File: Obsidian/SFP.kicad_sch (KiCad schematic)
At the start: 82 parts, among them J1 TYCO_1888247-1, J11 TYCO_1888247-1, J12 TYCO_1888247-1, J13 TYCO_1888247-1, J8 2180739-1, J9 2180739-1, U17 TCA9535RTWR, U19 TCA9535RTWR, U26 PCA9546ARGV

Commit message: update with available components on LCSC
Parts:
- C19, C23, C27, C28, C35, C36, C37, C38: LCSC (none) -> C296720
- C20, C21, C22, C220, C221, C222, C24, C25, C26, C29, C30, C31, C32, C33, C34, C39, C40, C41, C42: LCSC (none) -> C110251
- J1, J11, J12, J13: LCSC (none) -> C305914
- J8, J9: LCSC (none) -> C42931391
- L2, L3, L4, L5, L6, L7, L8, L9: LCSC (none) -> C82314
- R122, R21, R22, R23, R24, R25, R26, R27, R28, R29, R30, R31, R32, R33, R34, R35, R36, R37, R38, R39, R40, R41, R42, R43, R44, R45, R46, R47, R48: LCSC (none) -> C25900
- R164, R165, R166, R170, R171, R172, R173, R174, R175: LCSC (none) -> C60491
- U17, U19: FT Rotation Offset (none) -> 0; LCSC (none) -> C140277
- U26: FT Rotation Offset (none) -> 0; LCSC (none) -> C2649403

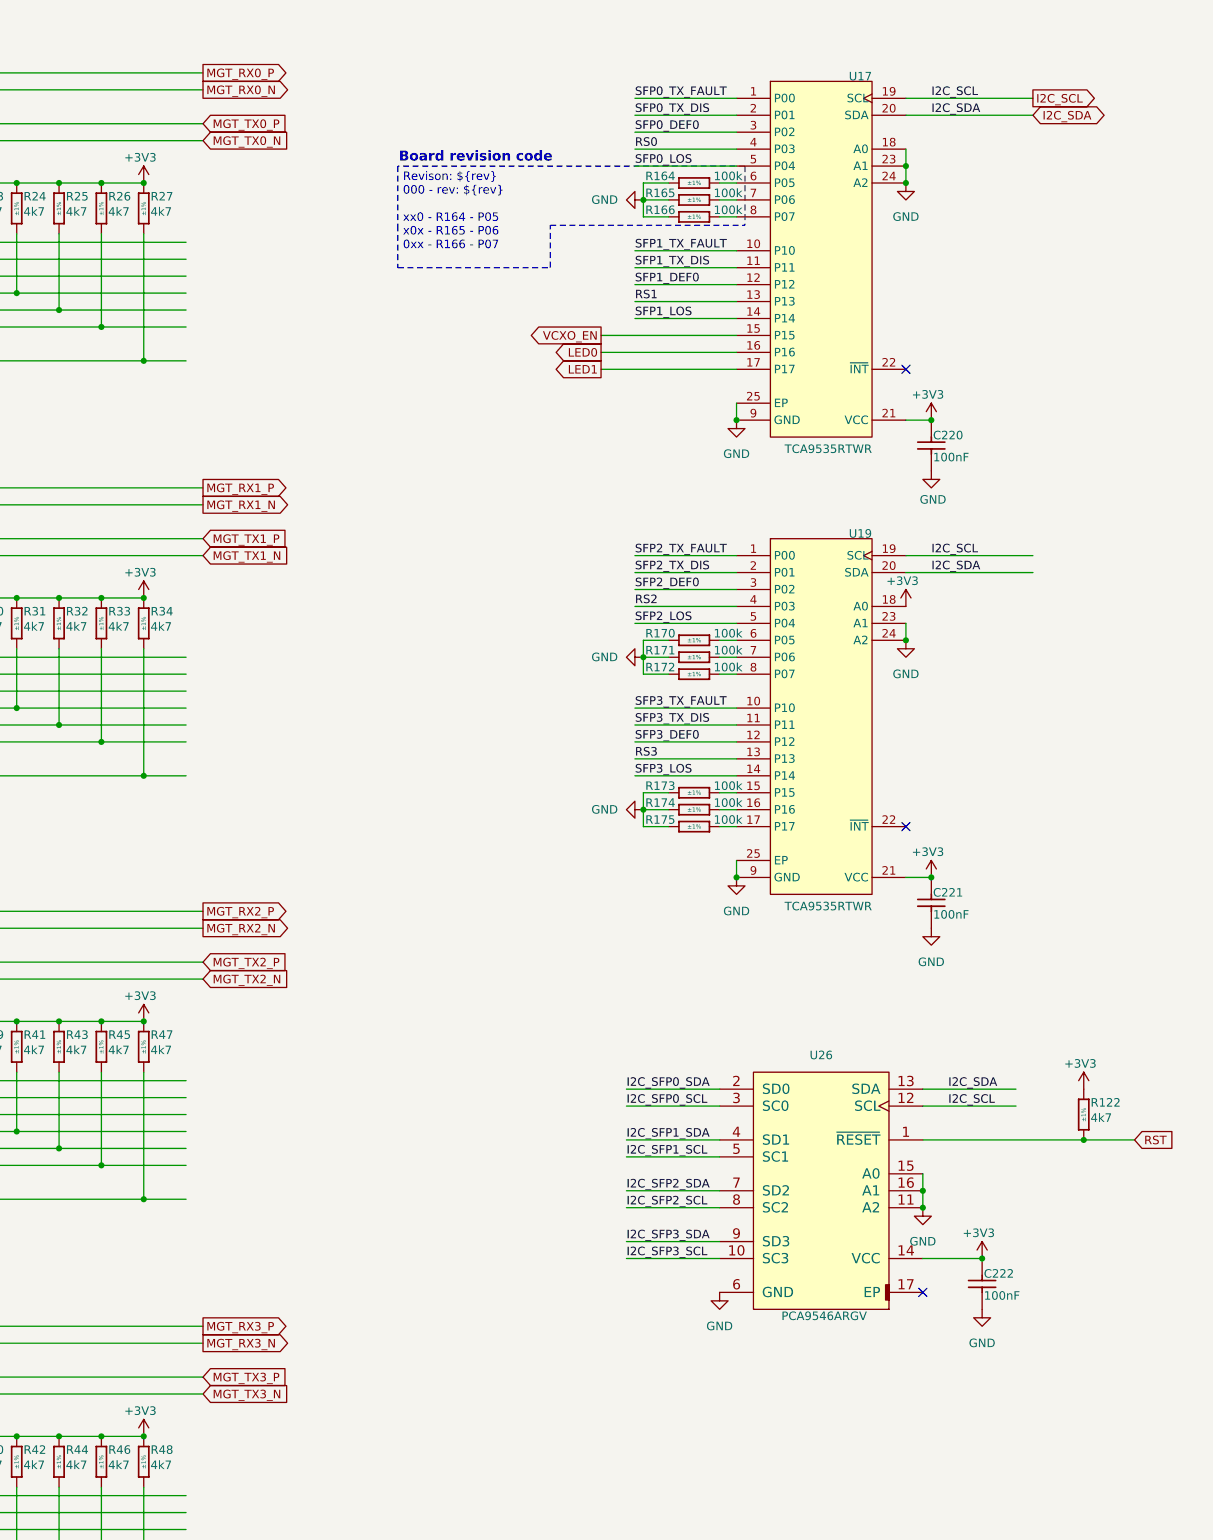
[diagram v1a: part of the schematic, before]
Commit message: replacing global label with hierarchical label
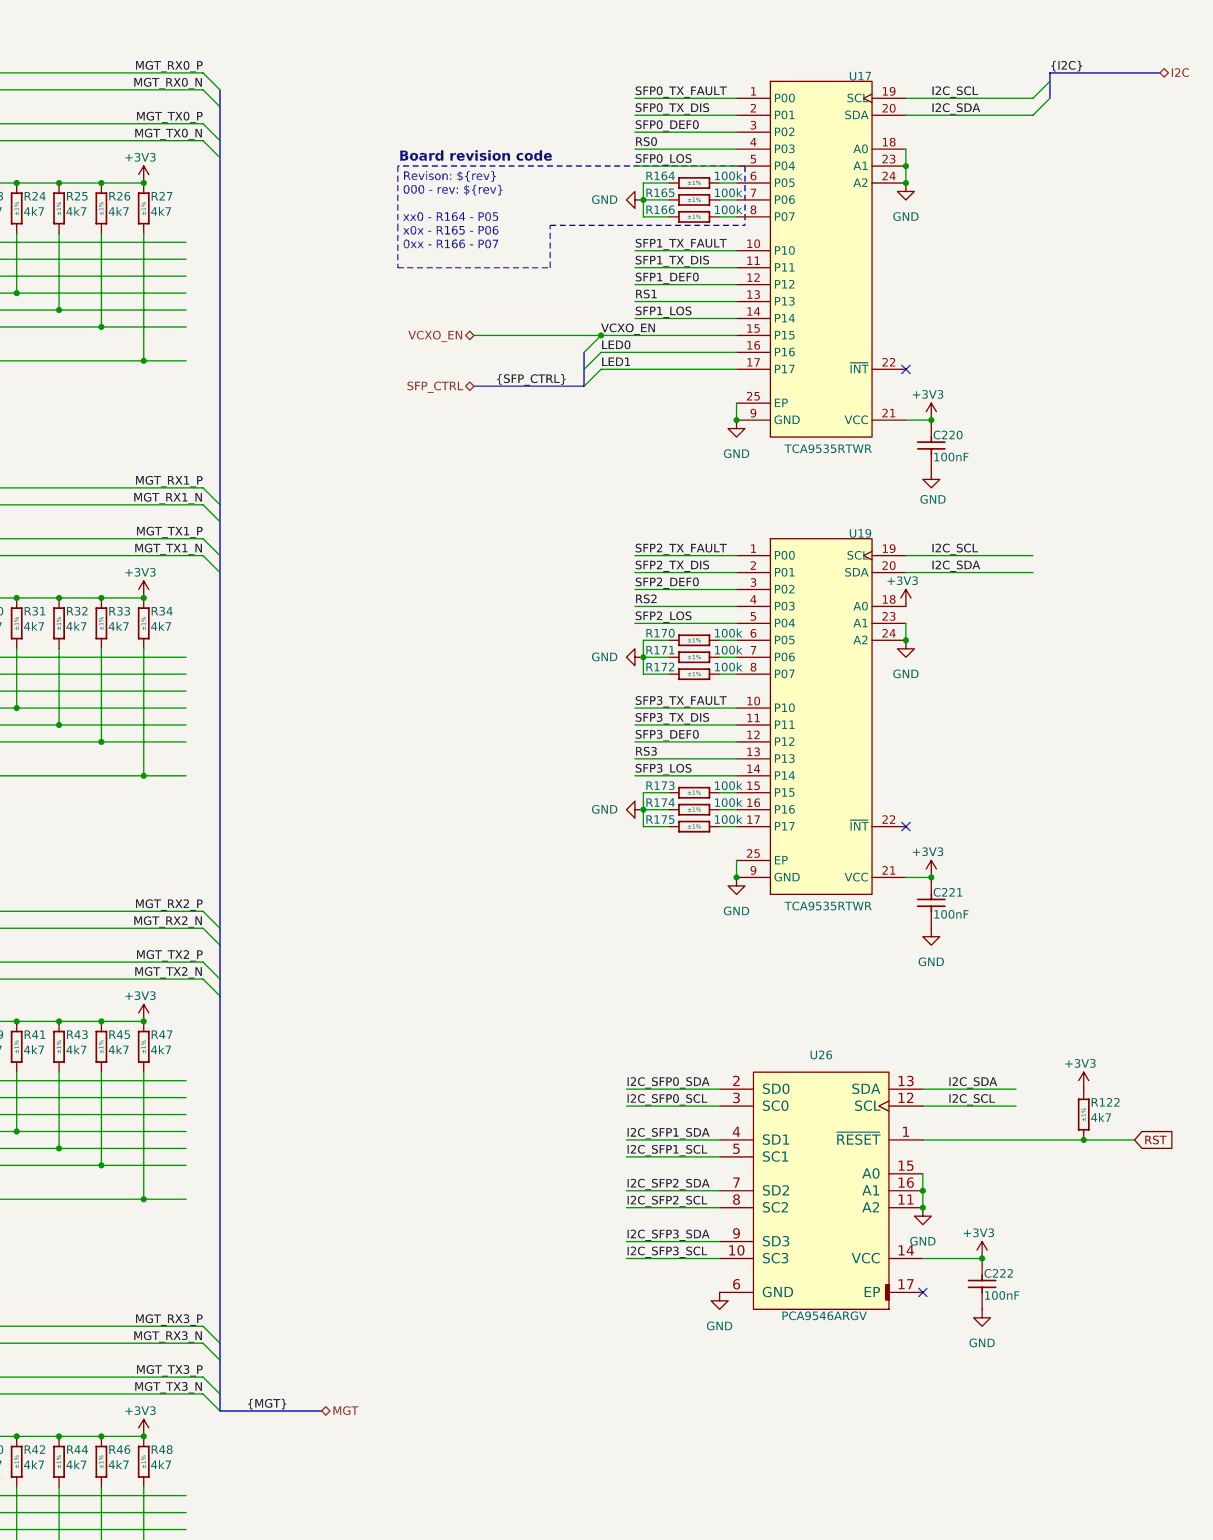
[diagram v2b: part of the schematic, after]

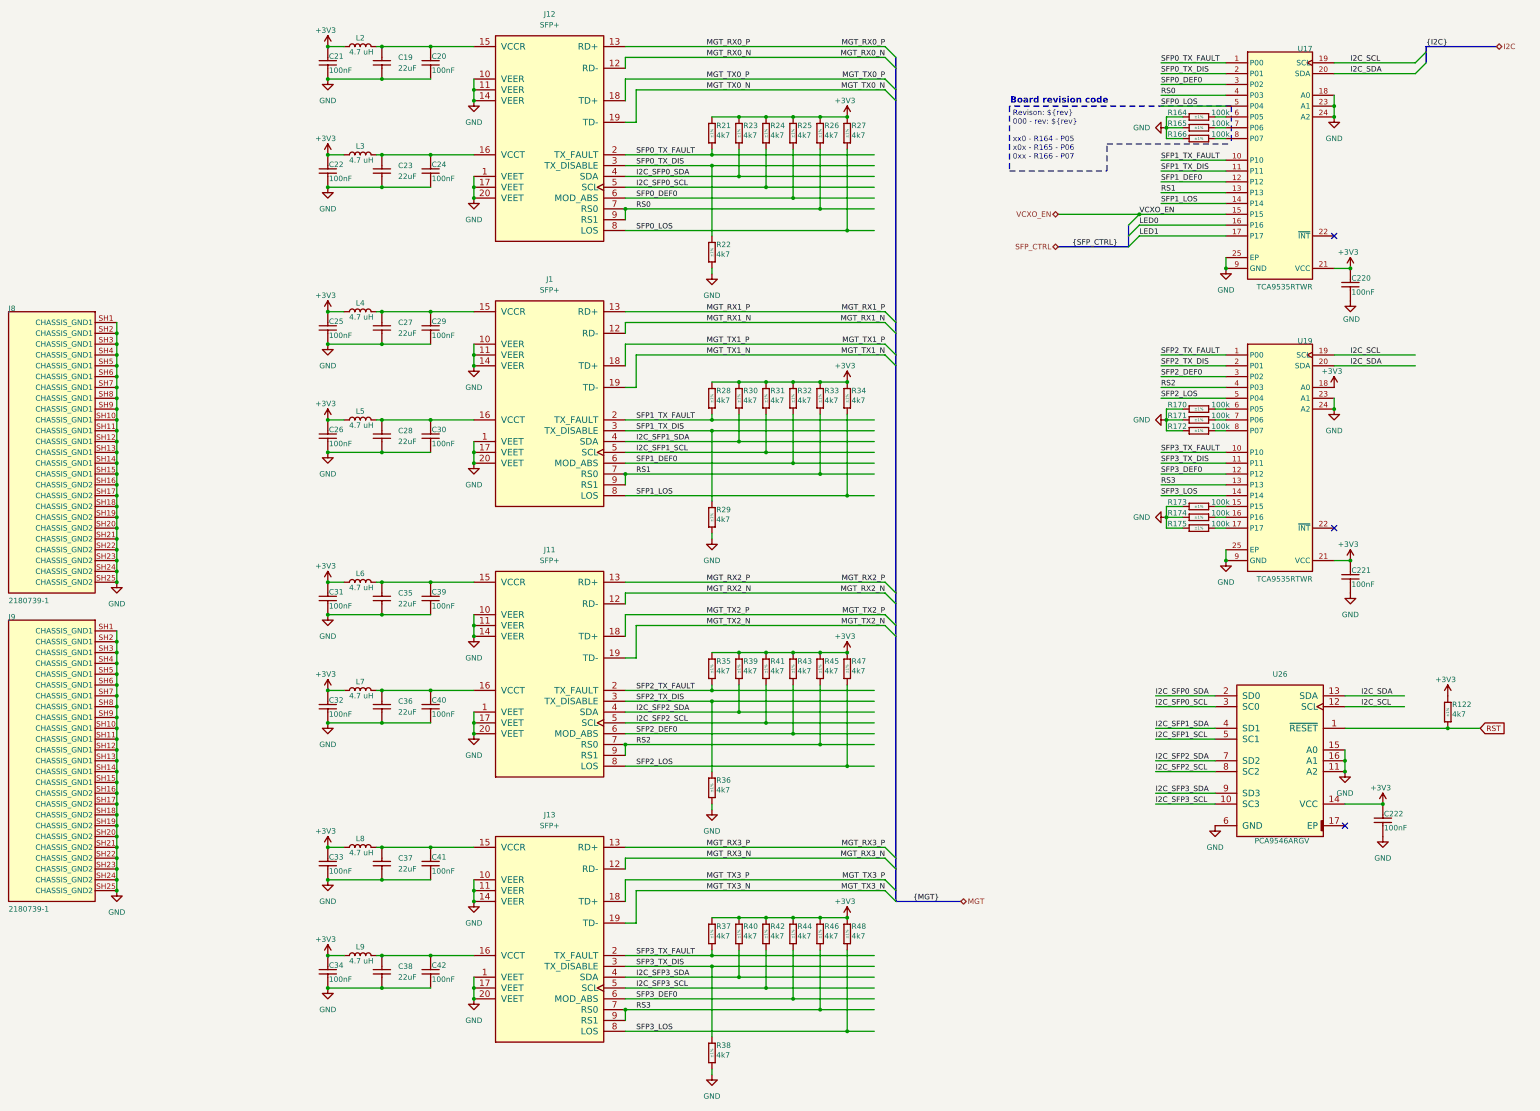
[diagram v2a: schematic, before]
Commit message: Adding symbol library
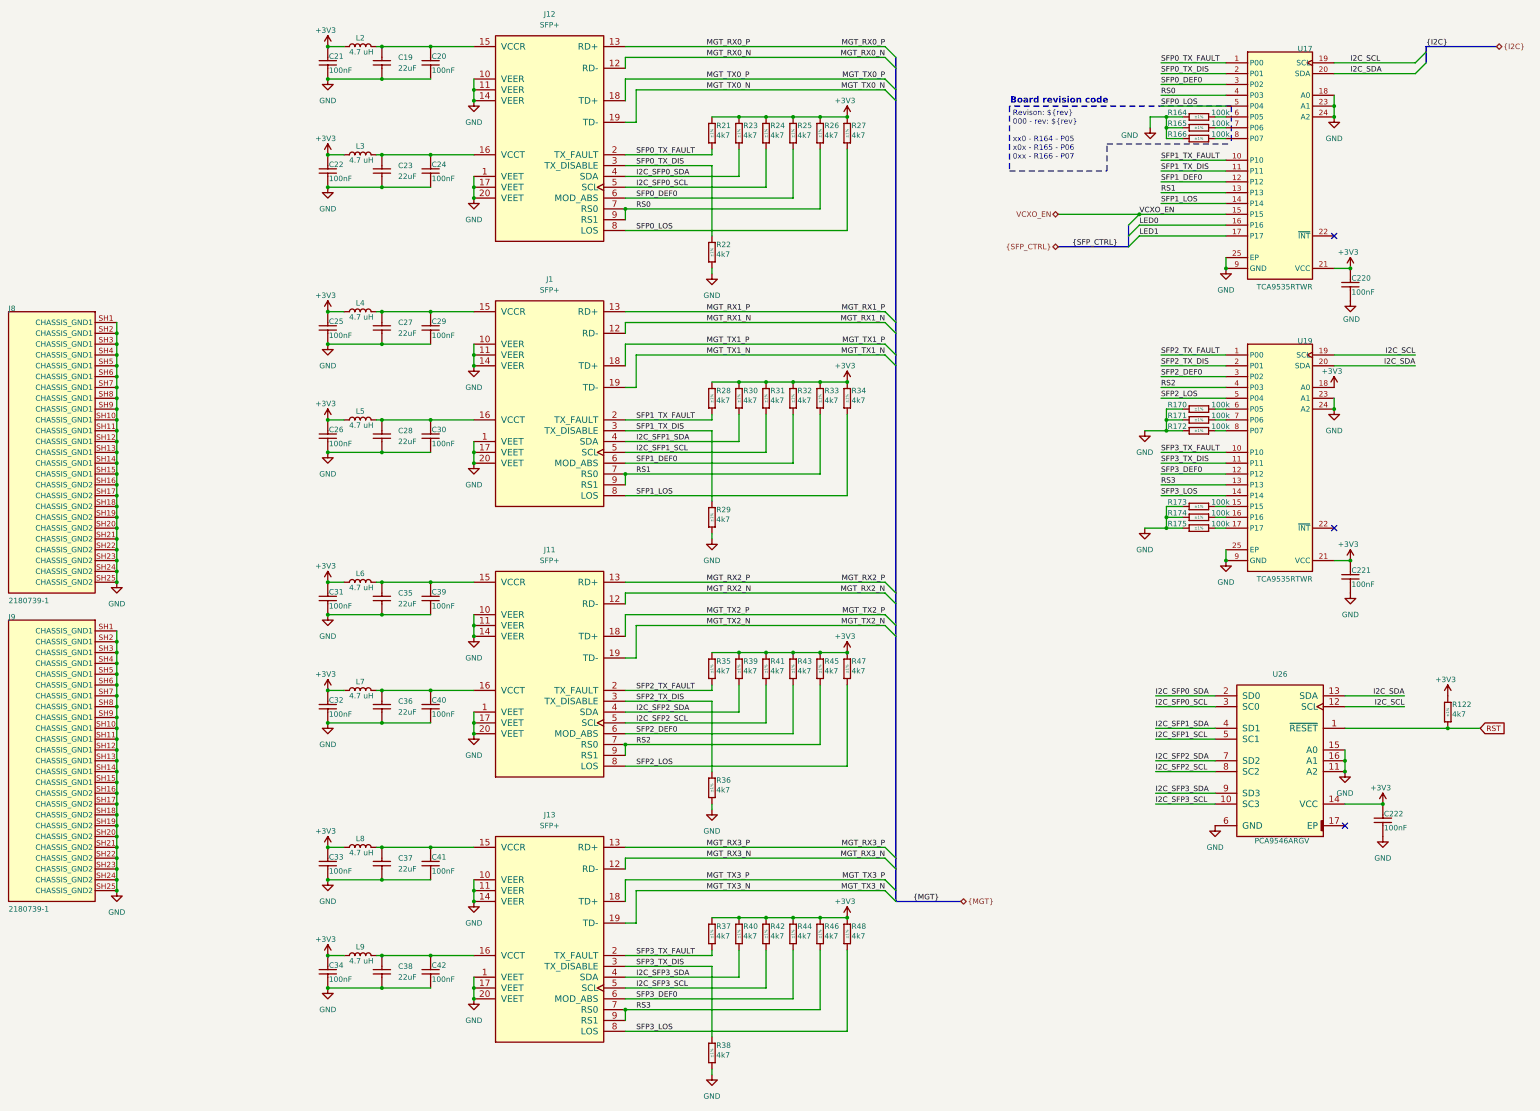
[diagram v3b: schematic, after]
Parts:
- C19, C23, C27, C28, C35, C36, C37, C38: symbol Capacitors SMD:CC0805_22UF_16V_10%_X5R -> Library_Symbol:CC0805_22UF_16V_10%_X5R
- C20, C21, C22, C220, C221, C222, C24, C25, C26, C29, C30, C31, C32, C33, C34, C39, C40, C41, C42: symbol Capacitors SMD:CC0402_100NF_50V_10%_X7R -> Library_Symbol:CC0402_100NF_50V_10%_X7R
- J1, J11, J12, J13: symbol TYCO:TYCO_1888247-1 -> Library_Symbol:TYCO_1888247-1
- J8, J9: symbol Sheet2-altium-import:root_0_2180739-1 -> Library_Symbol:root_0_2180739-1
- L2, L3, L4, L5, L6, L7, L8, L9: symbol Device:L -> Library_Symbol:L
- R122, R21, R22, R23, R24, R25, R26, R27, R28, R29, R30, R31, R32, R33, R34, R35, R36, R37, R38, R39, R40, R41, R42, R43, R44, R45, R46, R47, R48: symbol Resistors SMD:R0402_4K7_1%_0.0625W_100PPM -> Library_Symbol:R0402_4K7_1%_0.0625W_100PPM
- R164, R165, R166, R170, R171, R172, R173, R174, R175: symbol Resistors SMD:R0402_100K_1%_0.0625W_100PPM -> Library_Symbol:R0402_100K_1%_0.0625W_100PPM
- U17, U19: symbol Sheet3-altium-import:root_0_TI-TCA9535-QFN_RTW-24 -> Library_Symbol:root_0_TI-TCA9535-QFN_RTW-24
- U26: symbol Analog & Interface:PCA9546ARGV -> Library_Symbol:PCA9546ARGV

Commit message: Correct Schematic errors
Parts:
- C19, C23, C27, C28, C35, C36, C37, C38: footprint Capacitors SMD:CAPC2012X135N -> Footprint:CAPC2012X135N
- C20, C21, C22, C220, C221, C222, C24, C25, C26, C29, C30, C31, C32, C33, C34, C39, C40, C41, C42: footprint Capacitors SMD:CAPC1005X55N -> Footprint:CAPC1005X55N
- J1, J11: footprint TYCO SMD:TYCO_1888247-1 -> Footprint:TYCO_1367073-1
- J12, J13: footprint TYCO SMD:TYCO_1888247-1 -> Footprint:TYCO_1888247-1
- J8, J9: footprint TE_2180739-1 -> Footprint:TE_2180739-1
- L2, L3, L4, L5, L6, L7, L8, L9: footprint Inductor_SMD:L_1008_2520Metric -> Footprint:L_1008_2520Metric
- R122, R164, R165, R166, R170, R171, R172, R173, R174, R175, R21, R22, R23, R24, R25, R26, R27, R28, R29, R30, R31, R32, R33, R34, R35, R36, R37, R38, R39, R40, R41, R42, R43, R44, R45, R46, R47, R48: footprint Resistors SMD:RESC1005X40N -> Footprint:RESC1005X40N
- U17, U19: footprint ICs And Semiconductors SMD:QFN50P400X400X80-25N-S245 -> Footprint:QFN50P400X400X80-25N-S245
- U26: footprint ICs And Semiconductors SMD:QFN65P400X400X100-17N-S225 -> Footprint:QFN65P400X400X100-17N-S225

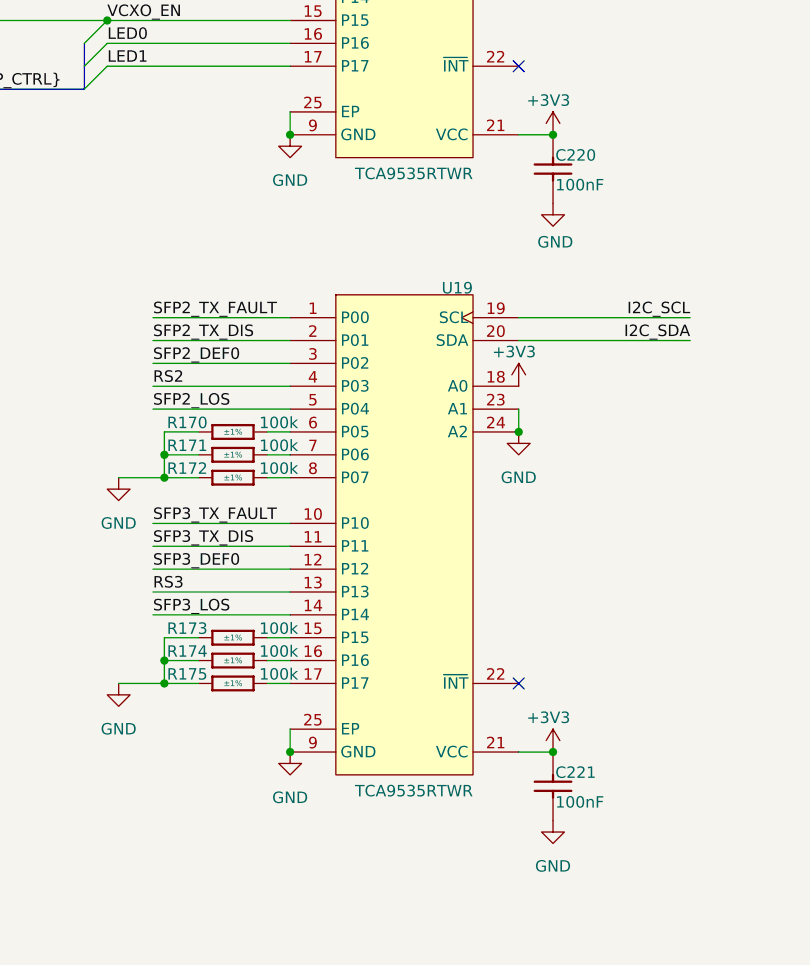
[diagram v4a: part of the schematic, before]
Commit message: adding 3D files, 3D model of twist, and correct DRC
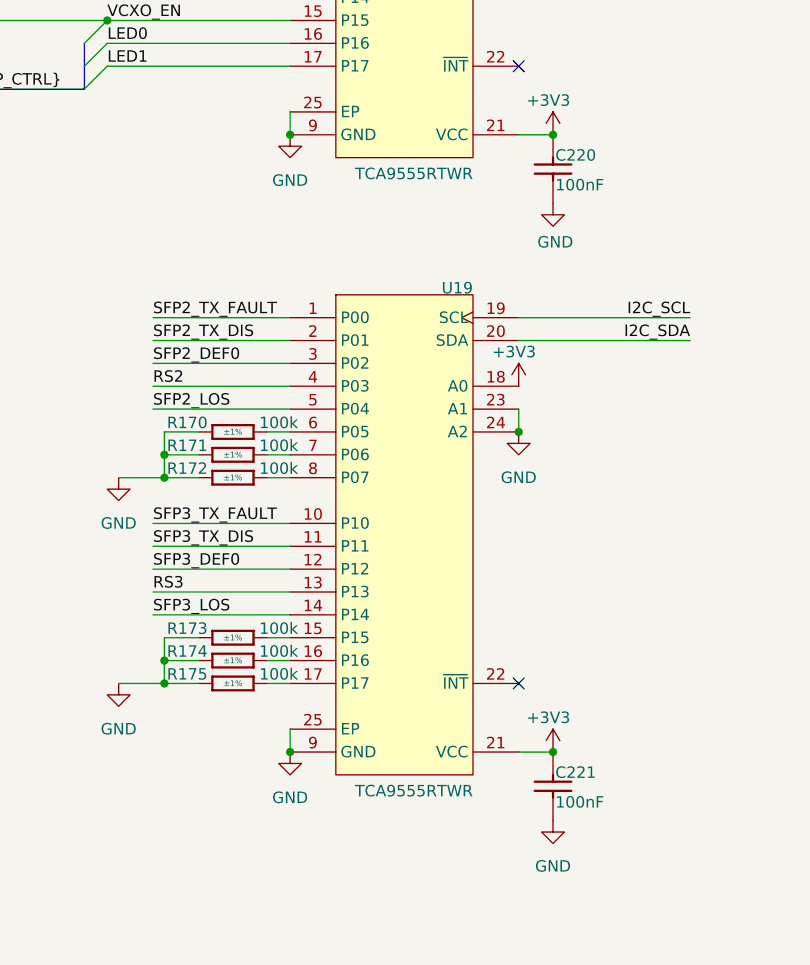
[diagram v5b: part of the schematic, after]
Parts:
- C20, C21, C22, C220, C221, C222, C24, C25, C26, C29, C30, C31, C32, C33, C34, C39, C40, C41, C42: footprint Footprint:CAPC1005X55N -> Capacitor_SMD:C_0402_1005Metric
- J1, J11: footprint Footprint:TYCO_1367073-1 -> Footprint:TYCO_1888247-1
- U17, U19: value TCA9535RTWR -> TCA9555RTWR
